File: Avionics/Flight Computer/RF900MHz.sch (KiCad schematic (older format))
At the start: 42 parts, among them J1 CONN_COAXIAL, J3 BMI-S-202-F, U1 CC1310F128RGZR, U2 CC1190RGVR

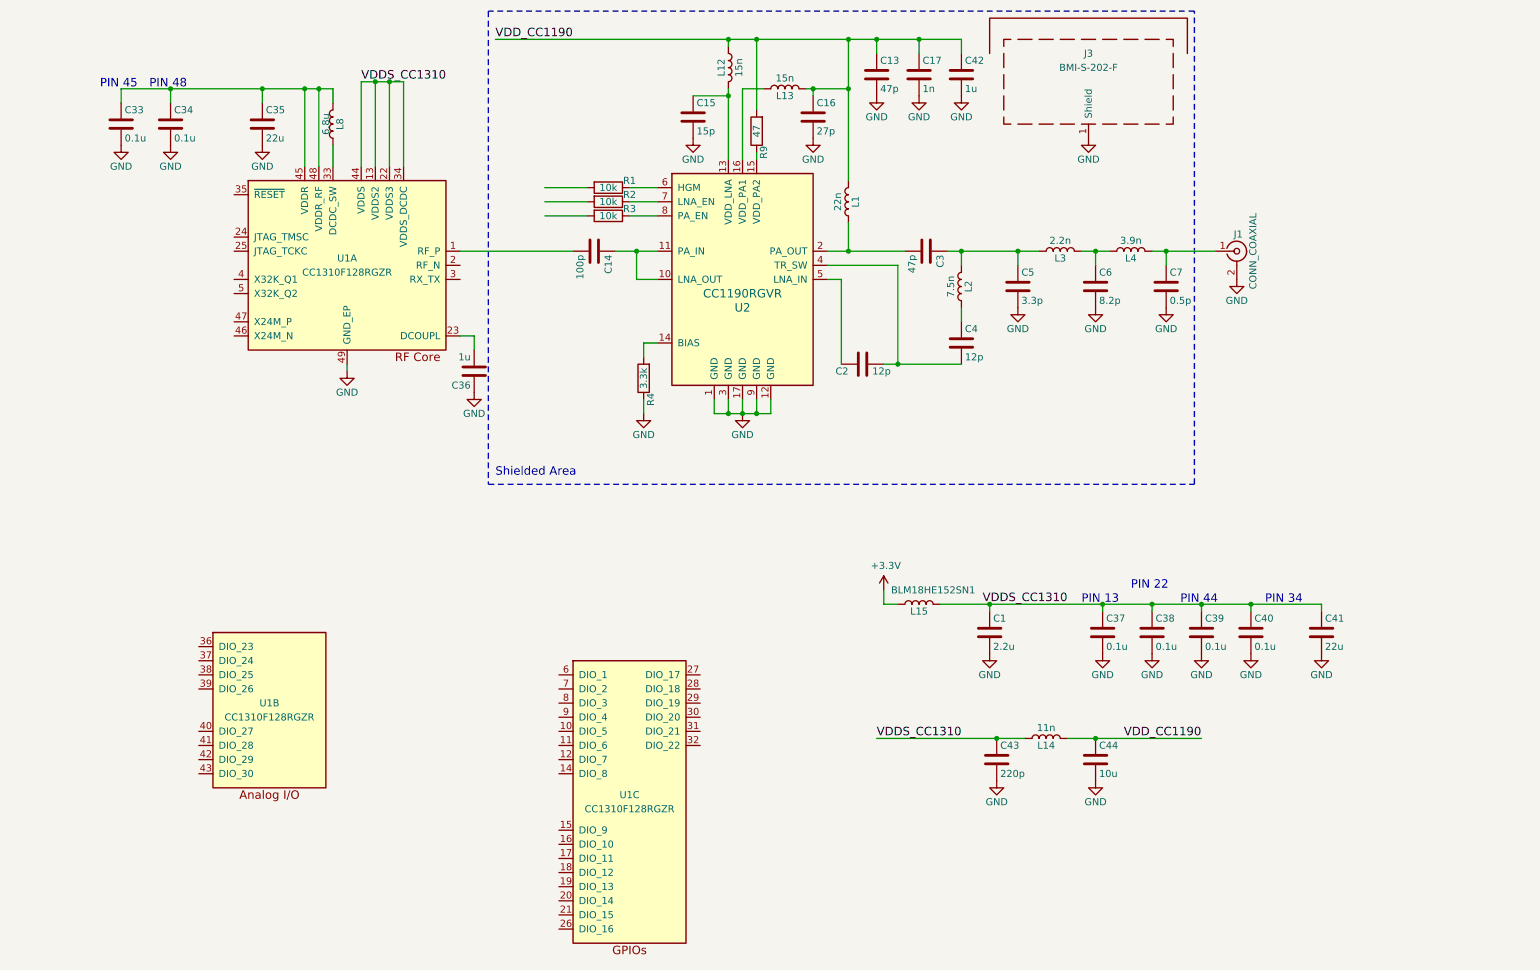
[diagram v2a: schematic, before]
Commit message: Restarted initial layout and cleaned up decoupling/RF layout.
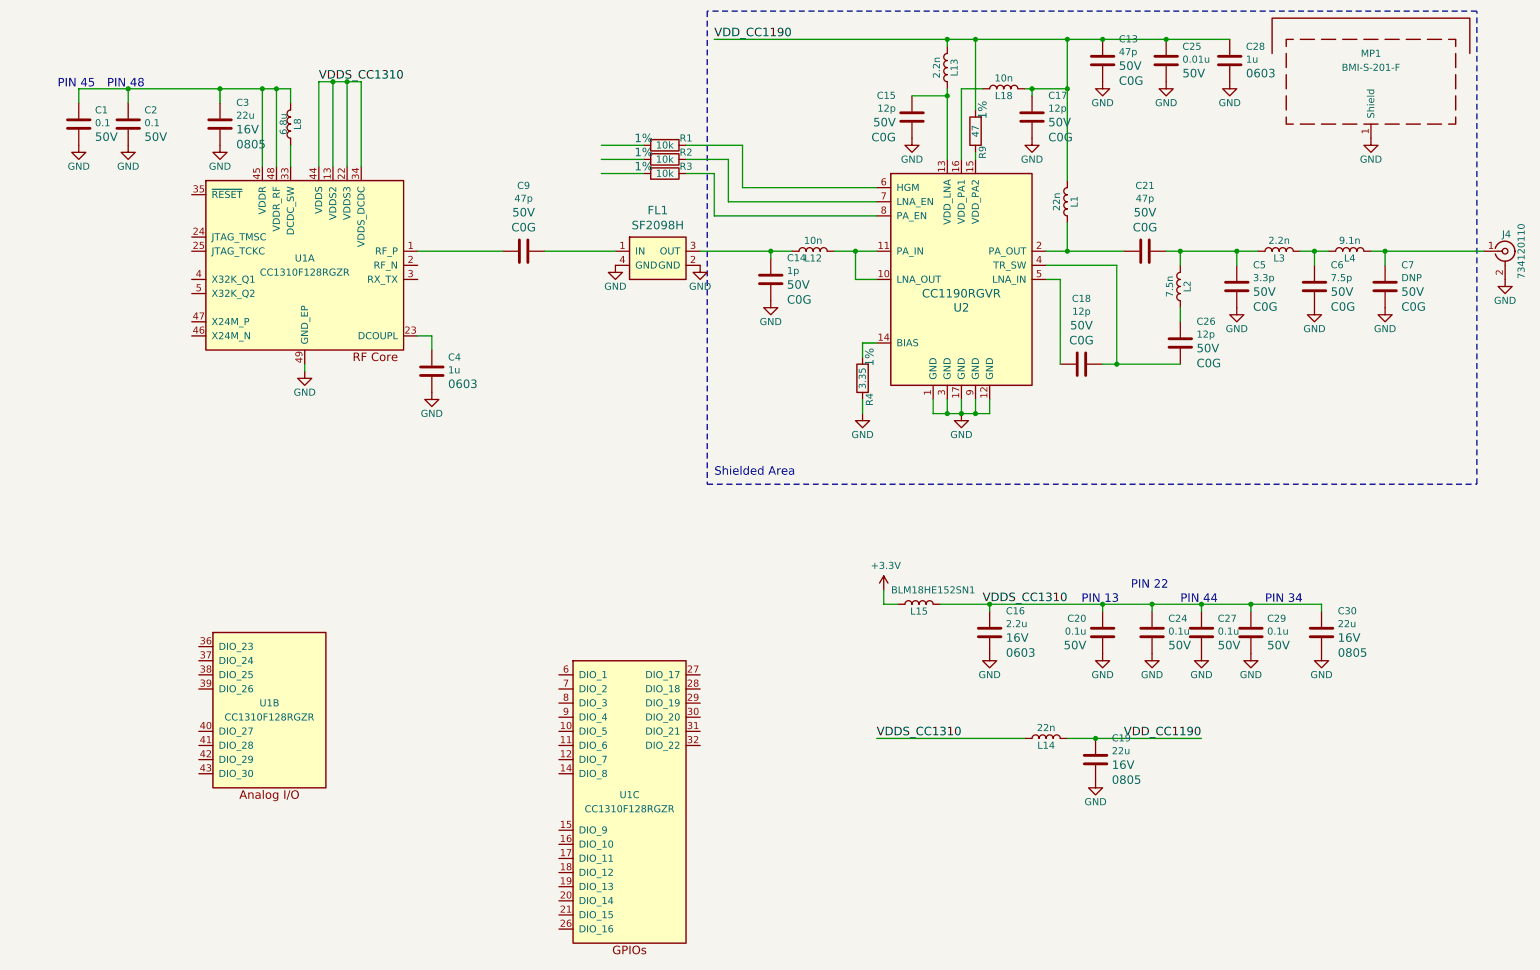
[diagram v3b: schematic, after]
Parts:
- removed C33, C34, C37, C38, C39, C40: 0.1u, Capacitors_SMD:C_0402, symbol C
- removed C35, C41: 22u, Capacitors_SMD:C_0603, symbol C
- removed C36, C42: 1u, Capacitors_SMD:C_0402, symbol C
- removed C43: 220p, Capacitors_SMD:C_0402, symbol C
- removed C44: 10u, Capacitors_SMD:C_0603, symbol C
- added C18, C26: 12p, Capacitors_SMD:C_0402, symbol C
- added C19, C30: 22u, Capacitors_SMD:C_0805, symbol C
- added C20, C24, C27, C29: 0.1u, Capacitors_SMD:C_0402, symbol C
- added C21, C9: 47p, Capacitors_SMD:C_0402, symbol C
- added C25: 0.01u, Capacitors_SMD:C_0402, symbol C
- added C28: 1u, Capacitors_SMD:C_0603, symbol C
- added FL1: SF2098H, SMD_Packages:SM2016-4, symbol SF2098H
- added L18: 10n, Inductors_SMD:L_0402, symbol L
- C1: value 2.2u -> 0.1; footprint Capacitors_SMD:C_0603 -> Capacitors_SMD:C_0402; Package (none) -> 0402; Tolerance (none) -> 20%; Type (none) -> X7R; Voltage (none) -> 50V
- C13, C5: Package (none) -> 0402; Tolerance (none) -> 20%; Type (none) -> C0G; Voltage (none) -> 50V
- C14: value 100p -> 1p; Package (none) -> 0402; Tolerance (none) -> 20%; Type (none) -> C0G; Voltage (none) -> 50V
- C15: value 15p -> 12p; Package (none) -> 0402; Tolerance (none) -> 20%; Type (none) -> C0G; Voltage (none) -> 50V
- C16: value 27p -> 2.2u; footprint Capacitors_SMD:C_0402 -> Capacitors_SMD:C_0603; Package (none) -> 0603; Tolerance (none) -> 20%; Type (none) -> X7R; Voltage (none) -> 16V
- C17: value 1n -> 12p; Package (none) -> 0402; Tolerance (none) -> 20%; Type (none) -> C0G; Voltage (none) -> 50V
- C2: value 12p -> 0.1; Package (none) -> 0402; Tolerance (none) -> 20%; Type (none) -> X7R; Voltage (none) -> 50V
- C3: value 47p -> 22u; footprint Capacitors_SMD:C_0402 -> Capacitors_SMD:C_0805; Package (none) -> 0805; Tolerance (none) -> 20%; Type (none) -> X7R; Voltage (none) -> 16V
- C4: value 12p -> 1u; footprint Capacitors_SMD:C_0402 -> Capacitors_SMD:C_0603; Package (none) -> 0603; Tolerance (none) -> 20%; Type (none) -> X7R; Voltage (none) -> 50V
- C6: value 8.2p -> 7.5p; Package (none) -> 0402; Tolerance (none) -> 20%; Type (none) -> C0G; Voltage (none) -> 50V
- C7: value 0.5p -> DNP; Package (none) -> 0402; Tolerance (none) -> 20%; Type (none) -> C0G; Voltage (none) -> 50V
- J4: renamed from J1; value CONN_COAXIAL -> 734120110
- L12: value 15n -> 10n
- L13: value 15n -> 2.2n
- L14: value 11n -> 22n
- L4: value 3.9n -> 9.1n
- MP1: renamed from J3; value BMI-S-202-F -> BMI-S-201-F; footprint Shielding_Cabinets:Laird_Technologies_BMI-S-202-F_16.50x16.50mm -> Shielding_Cabinets:Laird_Technologies_BMI-S-201-F_13.66x12.70mm
- R1, R2, R3, R9: Material (none) -> Thin Film; Package (none) -> 0402; Power (none) -> 0.062W; Tolerance (none) -> 1%; Voltage (none) -> 50V
- R4: value 3.3k -> 3.35; Material (none) -> Thin Film; Package (none) -> 0402; Power (none) -> 0.062W; Tolerance (none) -> 1%; Voltage (none) -> 50V
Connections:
- wire segments 75 -> 81
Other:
- moved on the sheet: J4, L1, L2, L3, L4, L8, MP1, U1A, U2

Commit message: Nearly completed initial placement.
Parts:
- added C66, C67: 12p, Capacitors_SMD:C_0402, symbol C
- added Y3: XRCGB24M000F2P00R0, Crystals:Crystal_SMD_2016-4pin_2.0x1.6mm, symbol Crystal_GND24
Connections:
- net labels added: HGM, LNA_EN, PA_EN, RF50_900_1, RF50_900_2, RF50_900_3, RF50_900_4, RF50_900_5, RF50_900_6, RF50_900_7, RF50_900_ANT, RF50_900_LNA, RF50_900_PA, RF50_900_TR, SSI0-CLK, SSI0-FSS, SSI0-RX, SSI0-TX, UART0-RX, UART0-TX, VDDR_CC1310
- wire segments 81 -> 99
- no-connect marks 0 -> 4
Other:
- moved on the sheet: C1, C2, C3, C4, C9, L8, U1A

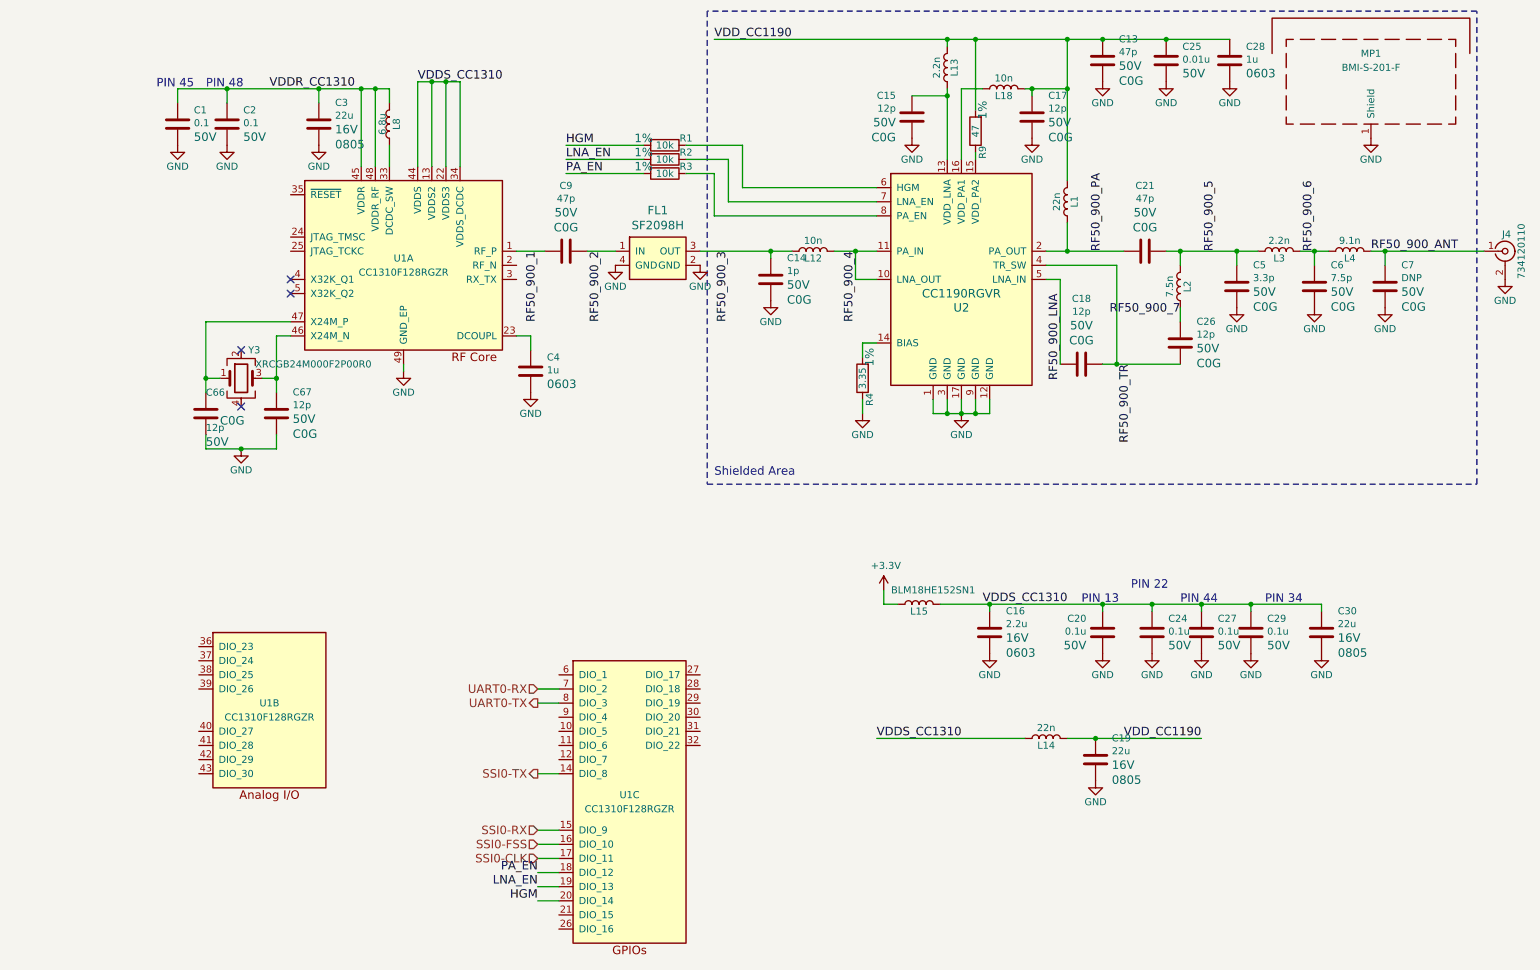
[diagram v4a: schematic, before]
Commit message: Added additional pinout
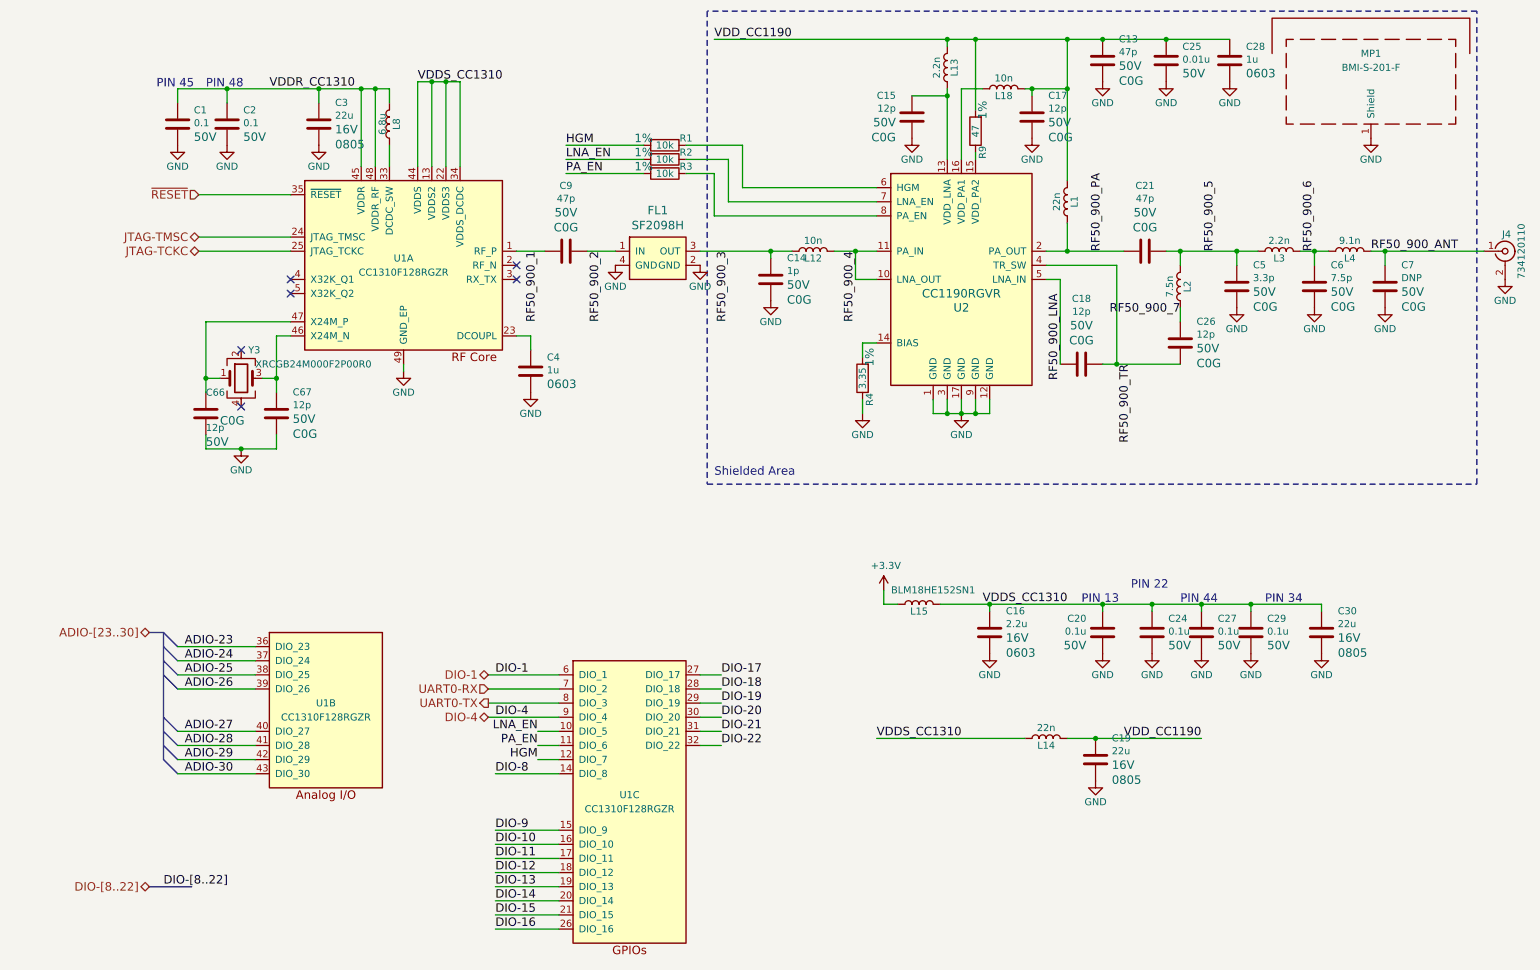
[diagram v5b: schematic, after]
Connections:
- net labels added: ADIO-23, ADIO-24, ADIO-25, ADIO-26, ADIO-27, ADIO-28, ADIO-29, ADIO-30, ADIO-[23..30], DIO-1, DIO-10, DIO-11, DIO-12, DIO-13, DIO-14, DIO-15, DIO-16, DIO-17, DIO-18, DIO-19, DIO-20, DIO-21, DIO-22, DIO-4, DIO-8, DIO-9, DIO-[8..22], JTAG-TCKC, JTAG-TMSC, ~RESET
- net labels removed: SSI0-CLK, SSI0-FSS, SSI0-RX, SSI0-TX
- wire segments 99 -> 123
- no-connect marks 4 -> 6
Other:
- moved on the sheet: U1B
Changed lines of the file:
@@
 L CC1310F128RGZR U1
 U 2 1 58AA1C24
-P 2150 5550
-F 0 "U1" H 2150 5600 50  0000 C CNN
-F 1 "CC1310F128RGZR" H 2150 5500 50  0000 C CNN
-F 2 "Housings_DFN_QFN:QFN-48-1EP_7x7mm_Pitch0.5mm" H 2150 5700 50  0001 C CNN
-F 3 "http://www.ti.com/lit/ds/symlink/cc1310.pdf" H 2150 5350 50  0001 C CNN
-	2    2150 5550
+P 2550 5550
+F 0 "U1" H 2550 5600 50  0000 C CNN
+F 1 "CC1310F128RGZR" H 2550 5500 50  0000 C CNN
+F 2 "Housings_DFN_QFN:QFN-48-1EP_7x7mm_Pitch0.5mm" H 2550 5700 50  0001 C CNN
+F 3 "http://www.ti.com/lit/ds/symlink/cc1310.pdf" H 2550 5350 50  0001 C CNN
+	2    2550 5550
 	1    0    0    -1
 $EndComp
@@
 NoConn ~ 2300 2500
 Wire Wire Line
-	4050 5400 4200 5400
-Text HLabel 4050 5400 0    60   Input ~ 0
+	3700 5400 4200 5400
+Text HLabel 3700 5400 0    60   Input ~ 0
 UART0-RX
 Wire Wire Line
-	4050 5500 4200 5500
-Text HLabel 4050 5500 0    60   Output ~ 0
+	3700 5500 4200 5500
+Text HLabel 3700 5500 0    60   Output ~ 0
 UART0-TX
-Wire Wire Line
-	4050 6500 4200 6500
-Text HLabel 4050 6500 0    60   Input ~ 0
-SSI0-FSS
-Wire Wire Line
-	4050 6600 4200 6600
-Text HLabel 4050 6600 0    60   Input ~ 0
-SSI0-CLK
-Wire Wire Line
-	4050 6000 4200 6000
-Text HLabel 4050 6000 0    60   Output ~ 0
-SSI0-TX
-Wire Wire Line
-	4050 6400 4200 6400
-Text HLabel 4050 6400 0    60   Input ~ 0
-SSI0-RX
 Text Label 2150 1150 0    60   ~ 0
 VDDR_CC1310
@@
 Text Label 4250 1750 0    60   ~ 0
 PA_EN
-Text Label 4050 6700 2    60   ~ 0
+Text Label 4050 5800 2    60   ~ 0
 PA_EN
-Text Label 4050 6800 2    60   ~ 0
+Text Label 4050 5700 2    60   ~ 0
 LNA_EN
-Text Label 4050 6900 2    60   ~ 0
+Text Label 4050 5900 2    60   ~ 0
 HGM
 Wire Wire Line
-	4050 6900 4200 6900
-Wire Wire Line
-	4200 6800 4050 6800
-Wire Wire Line
-	4050 6700 4200 6700
+	4050 5900 4200 5900
+Wire Wire Line
+	4200 5800 4050 5800
+Wire Wire Line
+	4050 5700 4200 5700
+Entry Bus Bus
+	1400 5900 1500 6000
+Entry Bus Bus
+	1400 5800 1500 5900
+Entry Bus Bus
+	1400 5700 1500 5800
+Entry Bus Bus
+	1400 5600 1500 5700
+Entry Bus Bus
+	1400 5300 1500 5400
+Entry Bus Bus
+	1400 5200 1500 5300
+Entry Bus Bus
+	1400 5100 1500 5200
+Entry Bus Bus
+	1400 5000 1500 5100
+Wire Bus Line
+	1400 5000 1400 5900
+Wire Bus Line
+	1400 5000 1300 5000
+Text HLabel 1300 5000 0    60   BiDi ~ 0
+ADIO-[23..30]
+Wire Wire Line
+	1500 5100 2050 5100
+Text Label 1550 5100 0    60   ~ 0
+ADIO-23
+Wire Wire Line
+	1500 5200 2050 5200
+Text Label 1550 5200 0    60   ~ 0
+ADIO-24
+Wire Wire Line
+	1500 5300 2050 5300
+Text Label 1550 5300 0    60   ~ 0
+ADIO-25
+Wire Wire Line
+	1500 5400 2050 5400
+Text Label 1550 5400 0    60   ~ 0
+ADIO-26
+Wire Wire Line
+	1500 5700 2050 5700
+Text Label 1550 5700 0    60   ~ 0
+ADIO-27
+Wire Wire Line
+	1500 5800 2050 5800
+Text Label 1550 5800 0    60   ~ 0
+ADIO-28
+Wire Wire Line
+	1500 5900 2050 5900
+Text Label 1550 5900 0    60   ~ 0
+ADIO-29
+Wire Wire Line
+	1500 6000 2050 6000
+Text Label 1550 6000 0    60   ~ 0
+ADIO-30
+Text HLabel 1650 1900 0    60   Input ~ 0
+~RESET
+Wire Wire Line
+	1650 1900 2300 1900
+Wire Wire Line
+	1650 2200 2300 2200
+Wire Wire Line
+	1650 2300 2300 2300
+Text HLabel 1650 2200 0    60   BiDi ~ 0
+JTAG-TMSC
+Text HLabel 1650 2300 0    60   BiDi ~ 0
+JTAG-TCKC
+Text HLabel 1300 6800 0    60   BiDi ~ 0
+DIO-[8..22]
+Wire Bus Line
+	1300 6800 1600 6800
+Text Label 1400 6800 0    60   ~ 0
+DIO-[8..22]
+Text Label 3750 6600 0    60   ~ 0
+DIO-11
+Wire Wire Line
+	3750 6600 4200 6600
+Wire Wire Line
+	3750 6700 4200 6700
+Wire Wire Line
+	3750 6800 4200 6800
+Text Label 3750 6700 0    60   ~ 0
+DIO-12
+Text Label 3750 6800 0    60   ~ 0
+DIO-13
+Text Label 3750 6900 0    60   ~ 0
+DIO-14
+Text Label 3750 7000 0    60   ~ 0
+DIO-15
+Text Label 3750 7100 0    60   ~ 0
+DIO-16
+Wire Wire Line
+	3750 6900 4200 6900
+Wire Wire Line
+	4200 7000 3750 7000
+Wire Wire Line
+	3750 7100 4200 7100
+Text Label 5350 5300 0    60   ~ 0
+DIO-17
+Text Label 5350 5400 0    60   ~ 0
+DIO-18
+Text Label 5350 5500 0    60   ~ 0
+DIO-19
+Text Label 5350 5600 0    60   ~ 0
+DIO-20
+Text Label 5350 5700 0    60   ~ 0
+DIO-21
+Text Label 5350 5800 0    60   ~ 0
+DIO-22
+Wire Wire Line
+	5200 5800 5350 5800
+Wire Wire Line
+	5350 5700 5200 5700
+Wire Wire Line
+	5200 5600 5350 5600
+Wire Wire Line
+	5350 5500 5200 5500
+Wire Wire Line
+	5200 5400 5350 5400
+Wire Wire Line
+	5350 5300 5200 5300
+NoConn ~ 3900 2400
+NoConn ~ 3900 2500
+Text Label 3750 5300 0    60   ~ 0
+DIO-1
+Wire Wire Line
+	3700 5300 4200 5300
+Text Label 3750 5600 0    60   ~ 0
+DIO-4
+Wire Wire Line
+	3700 5600 4200 5600
+Text Label 3750 6000 0    60   ~ 0
+DIO-8
+Wire Wire Line
+	3750 6000 4200 6000
+Text Label 3750 6400 0    60   ~ 0
+DIO-9
+Text Label 3750 6500 0    60   ~ 0
+DIO-10
+Wire Wire Line
+	3750 6400 4200 6400
+Wire Wire Line
+	4200 6500 3750 6500
+Text HLabel 3700 5600 0    60   BiDi ~ 0
+DIO-4
+Text HLabel 3700 5300 0    60   BiDi ~ 0
+DIO-1
 $EndSCHEMATC
